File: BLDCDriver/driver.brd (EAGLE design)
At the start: 42 x 49.1 mm, 60 parts, among them Q2 SIZ240DT-T1-GE3, Q3 SIZ240DT-T1-GE3, Q4 SIZ240DT-T1-GE3, U1 QFN50P400X400X100-25NDRV8300D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, U2 AS5048A-HTSP-500, U3 MCP2562-E/SN, U4 SOP80P620X125-8N, X2 JST-XH-06-PIN-LONG-PAD

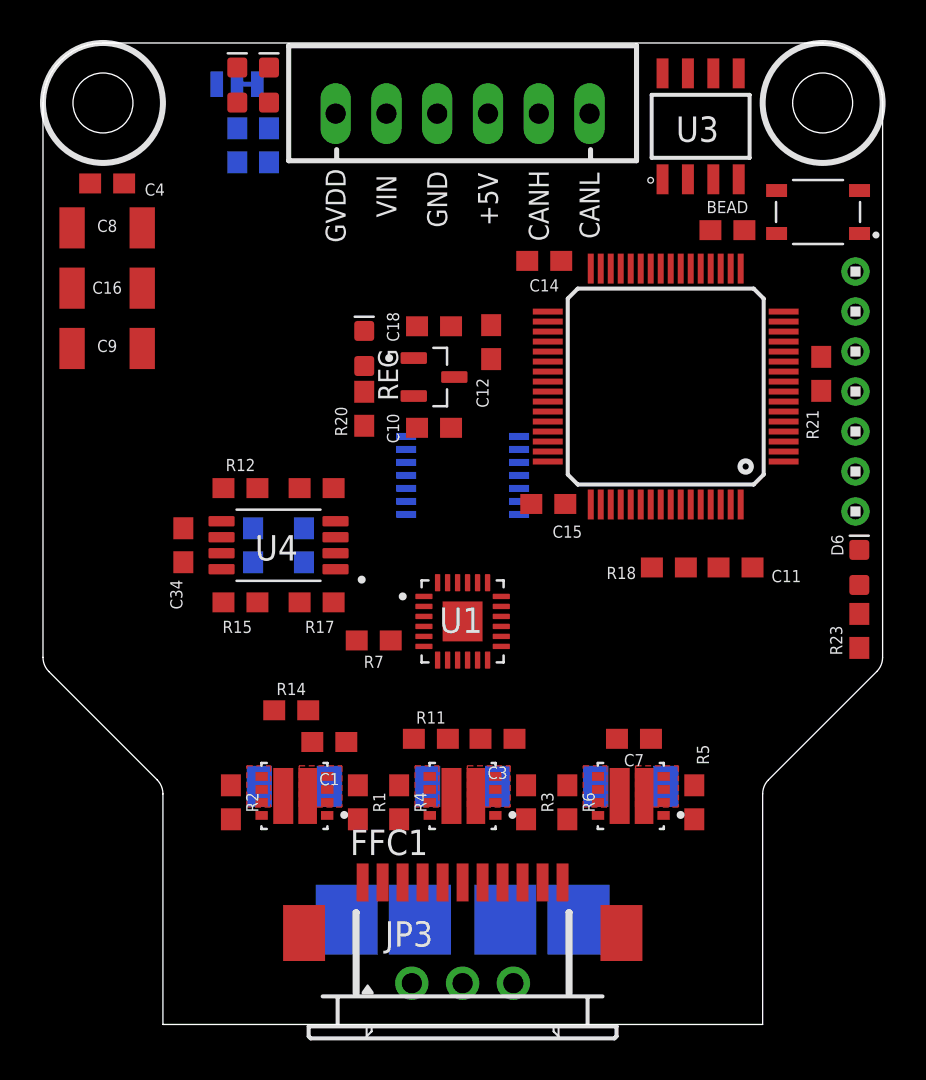
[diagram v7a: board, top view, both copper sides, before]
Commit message: 配置プロった
- コンデンサを追加した。
- 電流センシングの相をVからWに変えた
- パワーラインから配線はじめた
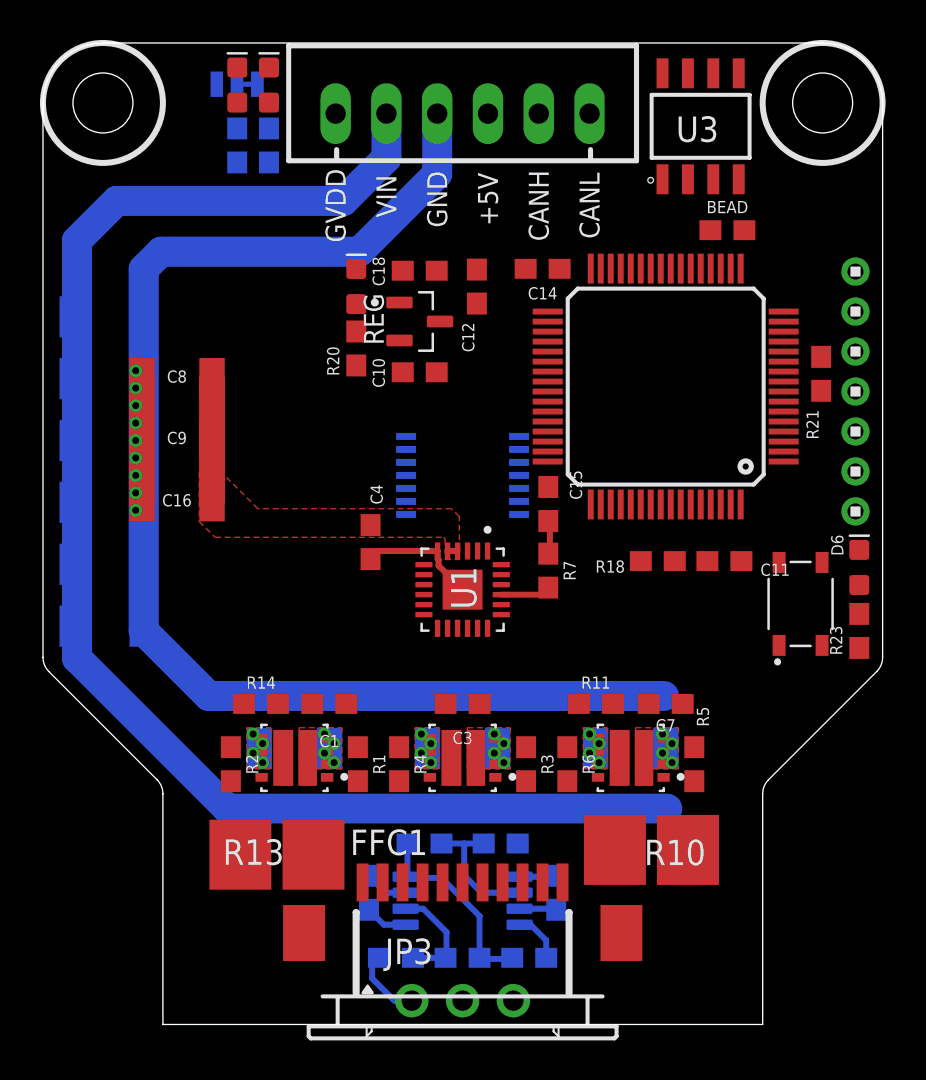
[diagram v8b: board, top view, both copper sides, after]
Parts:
- added C13, C17, C19, C20, C21, C22: 22UF-1210, SparkFun-Capacitors:1210
- moved C34 26.9 mm to (24.9, 5.24), flipped to the bottom, turned to 0 degrees
- moved R8 23.1 mm to (26.3, 8.49)
- moved C4 22.3 mm to (17.0, 26.0), turned to 270 degrees
- moved R12 22.0 mm to (23.5, 11.0), flipped to the bottom
- moved U4 20.0 mm to (21.6, 8.10), flipped to the bottom
- moved S1 19.6 mm to (38.5, 22.9), turned to 90 degrees
- moved R15 19.4 mm to (18.3, 5.24), flipped to the bottom, turned to 0 degrees
- moved R17 19.2 mm to (21.6, 5.24), flipped to the bottom, turned to 0 degrees
- moved R9 18.6 mm to (19.7, 11.0), flipped to the bottom
- moved R16 17.7 mm to (16.9, 8.49)
- moved C16 11.2 mm to (7.30, 28.1)
- moved R7 9.40 mm to (25.9, 24.6), turned to 270 degrees
- moved R11 8.44 mm to (28.3, 17.9)
- moved C8 8.31 mm to (7.30, 34.2)
- moved R10 6.50 mm to (31.0, 10.6), flipped to the top, turned to 180 degrees
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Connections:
- net C_V renamed C_W
- new net W_CS: FFC1.10, FFC1.11, R10.1, R12.2
- net GND: now also C13.1, C17.1, C19.1, C20.1, C21.1, C22.1
- net PVDD: now also C13.2, C17.2, C19.2, C20.2, C21.2, C22.2
- net V: now also FFC1.8, FFC1.9; no longer R10.2, R11.2
- net V_CS: no longer FFC1.8, FFC1.9, R10.1, R12.2
- net W: now also R10.2, R11.2; no longer FFC1.10, FFC1.11
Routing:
- net GND: track 0.00 -> 89.1 mm, vias 0 -> 21
- net PVDD: track 0.00 -> 72.9 mm, vias 0 -> 12
- net N$9: track 0.00 -> 6.83 mm
- net GVDD: track 0.00 -> 6.61 mm
- net N$11: track 0.00 -> 6.42 mm
- net U_CS: track 0.00 -> 3.62 mm
- net 3V3: track 0.00 -> 2.53 mm
- net DT: track 0.00 -> 2.50 mm
- net N$10: track 0.00 -> 2.18 mm
- net C_U: track 0.00 -> 2.14 mm
- net C_W: track 0.00 -> 1.86 mm
- net N$8: track 0.00 -> 1.85 mm
- added copper zone on layer 1, net GVDD
